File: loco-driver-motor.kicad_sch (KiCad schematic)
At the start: 20 parts, among them U901 BDR6133

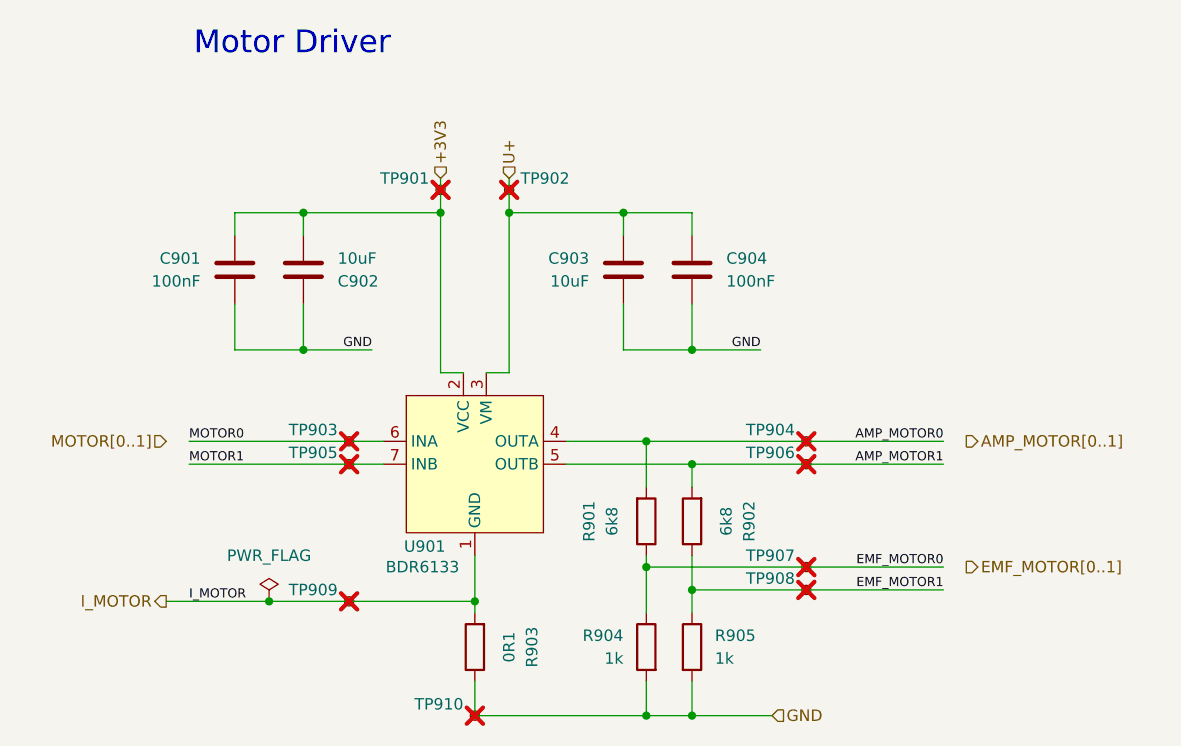
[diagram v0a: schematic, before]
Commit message: Fix - revert to working model
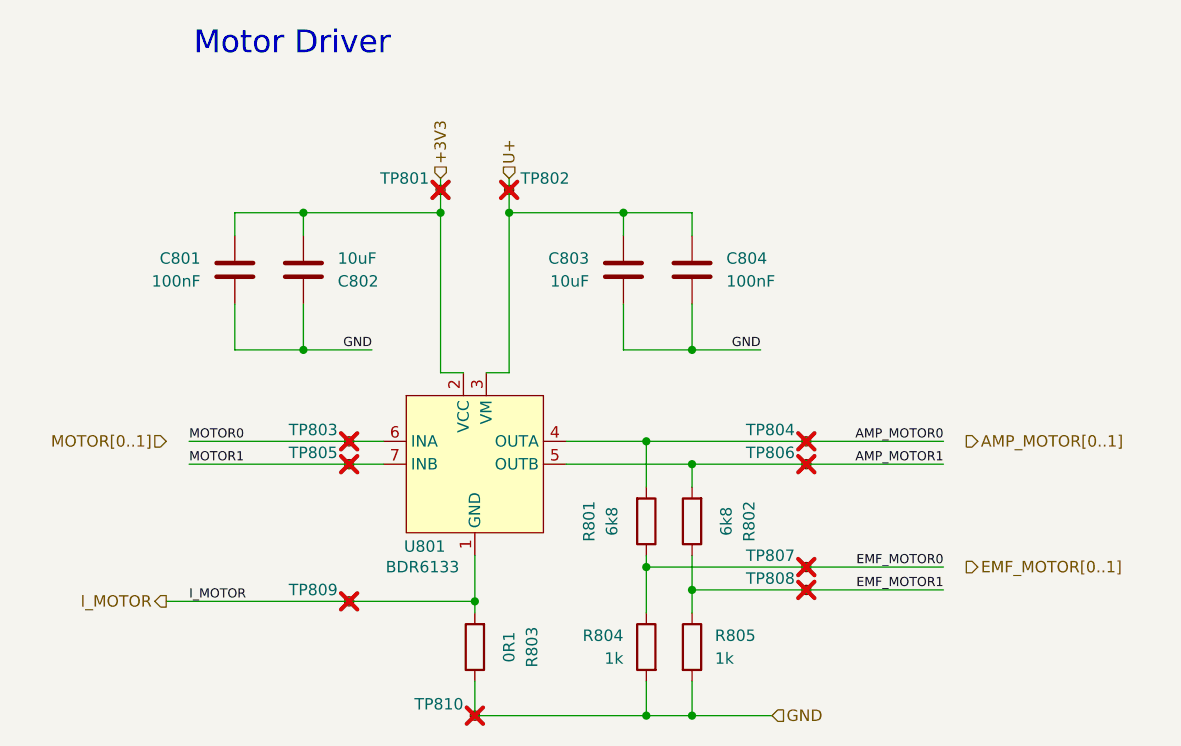
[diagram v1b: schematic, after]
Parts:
- renumbered C901 to C801, C902 to C802, C903 to C803, C904 to C804, R901 to R801, R902 to R802, R903 to R803, R904 to R804, R905 to R805, TP901 to TP801, TP902 to TP802, TP903 to TP803, TP904 to TP804, TP905 to TP805, TP906 to TP806, TP907 to TP807, TP908 to TP808, TP909 to TP809, TP910 to TP810, U901 to U801
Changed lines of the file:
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@@
-	)
-	(junction
-		(at 43.18 91.44)
-		(diameter 0)
-		(color 0 0 0 0)
 	)
 	(junction
@@
 	(wire
 		(pts
-			(xy 43.18 91.44) (xy 52.07 91.44)
-		)
-		(stroke
-			(width 0)
-			(type default)
-		)
-	)
-	(wire
-		(pts
 			(xy 66.04 100.33) (xy 66.04 104.14)
 		)
@@
 	(wire
 		(pts
-			(xy 31.75 91.44) (xy 43.18 91.44)
+			(xy 31.75 91.44) (xy 52.07 91.44)
 		)
 		(stroke
@@
 		(on_board no)
 		(dnp yes)
-		(property "Reference" "TP906"
+		(property "Reference" "TP806"
 			(at 101.6 74.9299 0)
 			(effects
@@
 			(project "xDuinoRails-Thor-M"
 				(path "/fb33ec4e-6596-45d2-a121-8d3475acd69a/28e0fa6a-354f-41d6-8b58-d1dd784eb1fe"
-					(reference "TP906")
+					(reference "TP806")
 					(unit 1)
 				)
@@
 		(on_board yes)
 		(dnp no)
-		(property "Reference" "U901"
+		(property "Reference" "U801"
 			(at 58.166 85.344 0)
 			(effects
@@
 			(project "xDuinoRails-Thor-M"
 				(path "/fb33ec4e-6596-45d2-a121-8d3475acd69a/28e0fa6a-354f-41d6-8b58-d1dd784eb1fe"
-					(reference "U901")
+					(reference "U801")
 					(unit 1)
 				)
@@
 		(on_board yes)
 		(dnp no)
-		(property "Reference" "R903"
+		(property "Reference" "R803"
 			(at 72.39 96.52 90)
 			(effects
@@
 			(project "xDuinoRails-Thor-M"
 				(path "/fb33ec4e-6596-45d2-a121-8d3475acd69a/28e0fa6a-354f-41d6-8b58-d1dd784eb1fe"
-					(reference "R903")
+					(reference "R803")
 					(unit 1)
 				)
@@
 		(on_board yes)
 		(dnp no)
-		(property "Reference" "R902"
+		(property "Reference" "R802"
 			(at 96.52 82.55 90)
 			(effects
@@
 			(project "xDuinoRails-Thor-M"
 				(path "/fb33ec4e-6596-45d2-a121-8d3475acd69a/28e0fa6a-354f-41d6-8b58-d1dd784eb1fe"
-					(reference "R902")
-					(unit 1)
-				)
-			)
-		)
-	)
-	(symbol
-		(lib_id "power:PWR_FLAG")
-		(at 43.18 91.44 0)
-		(unit 1)
-		(exclude_from_sim no)
-		(in_bom yes)
-		(on_board yes)
-		(dnp no)
-		(fields_autoplaced yes)
-		(property "Reference" "#FLG901"
-			(at 43.18 89.535 0)
-			(effects
-				(font
-					(size 1.27 1.27)
-				)
-				(hide yes)
-			)
-		)
-		(property "Value" "PWR_FLAG"
-			(at 43.18 86.36 0)
-			(effects
-				(font
-					(size 1.27 1.27)
-				)
-			)
-		)
-		(property "Footprint" ""
-			(at 43.18 91.44 0)
-			(effects
-				(font
-					(size 1.27 1.27)
-				)
-				(hide yes)
-			)
-		)
-		(property "Datasheet" "~"
-			(at 43.18 91.44 0)
-			(effects
-				(font
-					(size 1.27 1.27)
-				)
-				(hide yes)
-			)
-		)
-		(property "Description" "Special symbol for telling ERC where power comes from"
-			(at 43.18 91.44 0)
-			(effects
-				(font
-					(size 1.27 1.27)
-				)
-				(hide yes)
-			)
-		)
-		(pin "1"
-		)
-		(instances
-			(project ""
-				(path "/fb33ec4e-6596-45d2-a121-8d3475acd69a/28e0fa6a-354f-41d6-8b58-d1dd784eb1fe"
-					(reference "#FLG901")
+					(reference "R802")
 					(unit 1)
 				)
@@
 		(on_board no)
 		(dnp yes)
-		(property "Reference" "TP909"
+		(property "Reference" "TP809"
 			(at 50.8 90.1699 0)
 			(effects
@@
 			(project "xDuinoRails-Thor-M"
 				(path "/fb33ec4e-6596-45d2-a121-8d3475acd69a/28e0fa6a-354f-41d6-8b58-d1dd784eb1fe"
-					(reference "TP909")
+					(reference "TP809")
 					(unit 1)
 				)
@@
 		(dnp no)
 		(fields_autoplaced yes)
-		(property "Reference" "R901"
+		(property "Reference" "R801"
 			(at 78.74 82.55 90)
 			(effects
@@
 			(project "xDuinoRails-Thor-M"
 				(path "/fb33ec4e-6596-45d2-a121-8d3475acd69a/28e0fa6a-354f-41d6-8b58-d1dd784eb1fe"
-					(reference "R901")
+					(reference "R801")
 					(unit 1)
 				)
@@
 		(on_board no)
 		(dnp yes)
-		(property "Reference" "TP904"
+		(property "Reference" "TP804"
 			(at 101.6 72.3899 0)
 			(effects
@@
 			(project "xDuinoRails-Thor-M"
 				(path "/fb33ec4e-6596-45d2-a121-8d3475acd69a/28e0fa6a-354f-41d6-8b58-d1dd784eb1fe"
-					(reference "TP904")
+					(reference "TP804")
 					(unit 1)
 				)
@@
 		(on_board no)
 		(dnp yes)
-		(property "Reference" "TP908"
+		(property "Reference" "TP808"
 			(at 101.6 88.8999 0)
 			(effects
@@
 			(project "xDuinoRails-Thor-M"
 				(path "/fb33ec4e-6596-45d2-a121-8d3475acd69a/28e0fa6a-354f-41d6-8b58-d1dd784eb1fe"
-					(reference "TP908")
+					(reference "TP808")
 					(unit 1)
 				)
@@
 		(on_board no)
 		(dnp yes)
-		(property "Reference" "TP902"
+		(property "Reference" "TP802"
 			(at 71.12 44.4499 0)
 			(effects
@@
 			(project "xDuinoRails-Thor-M"
 				(path "/fb33ec4e-6596-45d2-a121-8d3475acd69a/28e0fa6a-354f-41d6-8b58-d1dd784eb1fe"
-					(reference "TP902")
+					(reference "TP802")
 					(unit 1)
 				)
@@
 		(dnp no)
 		(fields_autoplaced yes)
-		(property "Reference" "C904"
+		(property "Reference" "C804"
 			(at 93.98 53.3399 0)
 			(effects
@@
 			(project "xDuinoRails-Thor-M"
 				(path "/fb33ec4e-6596-45d2-a121-8d3475acd69a/28e0fa6a-354f-41d6-8b58-d1dd784eb1fe"
-					(reference "C904")
+					(reference "C804")
 					(unit 1)
 				)
@@
 		(on_board no)
 		(dnp yes)
-		(property "Reference" "TP901"
+		(property "Reference" "TP801"
 			(at 60.96 44.4499 0)
 			(effects
@@
 			(project "xDuinoRails-Thor-M"
 				(path "/fb33ec4e-6596-45d2-a121-8d3475acd69a/28e0fa6a-354f-41d6-8b58-d1dd784eb1fe"
-					(reference "TP901")
+					(reference "TP801")
 					(unit 1)
 				)
@@
 		(dnp no)
 		(fields_autoplaced yes)
-		(property "Reference" "R904"
+		(property "Reference" "R804"
 			(at 82.55 95.2499 0)
 			(effects
@@
 			(project "xDuinoRails-Thor-M"
 				(path "/fb33ec4e-6596-45d2-a121-8d3475acd69a/28e0fa6a-354f-41d6-8b58-d1dd784eb1fe"
-					(reference "R904")
+					(reference "R804")
 					(unit 1)
 				)
@@
 		(on_board no)
 		(dnp yes)
-		(property "Reference" "TP903"
+		(property "Reference" "TP803"
 			(at 50.8 72.3899 0)
 			(effects
@@
 			(project "xDuinoRails-Thor-M"
 				(path "/fb33ec4e-6596-45d2-a121-8d3475acd69a/28e0fa6a-354f-41d6-8b58-d1dd784eb1fe"
-					(reference "TP903")
+					(reference "TP803")
 					(unit 1)
 				)
@@
 		(on_board yes)
 		(dnp no)
-		(property "Reference" "C903"
+		(property "Reference" "C803"
 			(at 78.74 53.3399 0)
 			(effects
@@
 			(project "xDuinoRails-Thor-M"
 				(path "/fb33ec4e-6596-45d2-a121-8d3475acd69a/28e0fa6a-354f-41d6-8b58-d1dd784eb1fe"
-					(reference "C903")
+					(reference "C803")
 					(unit 1)
 				)
@@
 		(on_board no)
 		(dnp yes)
-		(property "Reference" "TP907"
+		(property "Reference" "TP807"
 			(at 101.6 86.3599 0)
 			(effects
@@
 			(project "xDuinoRails-Thor-M"
 				(path "/fb33ec4e-6596-45d2-a121-8d3475acd69a/28e0fa6a-354f-41d6-8b58-d1dd784eb1fe"
-					(reference "TP907")
+					(reference "TP807")
 					(unit 1)
 				)
@@
 		(on_board no)
 		(dnp yes)
-		(property "Reference" "TP910"
+		(property "Reference" "TP810"
 			(at 64.77 102.8699 0)
 			(effects
@@
 			(project "xDuinoRails-Thor-M"
 				(path "/fb33ec4e-6596-45d2-a121-8d3475acd69a/28e0fa6a-354f-41d6-8b58-d1dd784eb1fe"
-					(reference "TP910")
+					(reference "TP810")
 					(unit 1)
 				)
@@
 		(dnp no)
 		(fields_autoplaced yes)
-		(property "Reference" "C901"
+		(property "Reference" "C801"
 			(at 35.56 53.3399 0)
 			(effects
@@
 			(project "xDuinoRails-Thor-M"
 				(path "/fb33ec4e-6596-45d2-a121-8d3475acd69a/28e0fa6a-354f-41d6-8b58-d1dd784eb1fe"
-					(reference "C901")
+					(reference "C801")
 					(unit 1)
 				)
@@
 		(on_board yes)
 		(dnp no)
-		(property "Reference" "C902"
+		(property "Reference" "C802"
 			(at 50.8 55.8801 0)
 			(effects
@@
 			(project "xDuinoRails-Thor-M"
 				(path "/fb33ec4e-6596-45d2-a121-8d3475acd69a/28e0fa6a-354f-41d6-8b58-d1dd784eb1fe"
-					(reference "C902")
+					(reference "C802")
 					(unit 1)
 				)
@@
 		(on_board no)
 		(dnp yes)
-		(property "Reference" "TP905"
+		(property "Reference" "TP805"
 			(at 50.8 74.9299 0)
 			(effects
@@
 			(project "xDuinoRails-Thor-M"
 				(path "/fb33ec4e-6596-45d2-a121-8d3475acd69a/28e0fa6a-354f-41d6-8b58-d1dd784eb1fe"
-					(reference "TP905")
+					(reference "TP805")
 					(unit 1)
 				)
@@
 		(on_board yes)
 		(dnp no)
-		(property "Reference" "R905"
+		(property "Reference" "R805"
 			(at 92.71 95.2499 0)
 			(effects
@@
 			(project "xDuinoRails-Thor-M"
 				(path "/fb33ec4e-6596-45d2-a121-8d3475acd69a/28e0fa6a-354f-41d6-8b58-d1dd784eb1fe"
-					(reference "R905")
+					(reference "R805")
 					(unit 1)
 				)

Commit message: Add - Fix ERC errors
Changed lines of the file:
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@@
+	)
+	(junction
+		(at 54.61 91.44)
+		(diameter 0)
+		(color 0 0 0 0)
 	)
 	(junction
@@
 	(wire
 		(pts
-			(xy 52.07 91.44) (xy 66.04 91.44)
-		)
-		(stroke
-			(width 0)
-			(type default)
-		)
-	)
-	(wire
-		(pts
 			(xy 90.17 86.36) (xy 90.17 90.17)
 		)
@@
 	(wire
 		(pts
+			(xy 54.61 91.44) (xy 52.07 91.44)
+		)
+		(stroke
+			(width 0)
+			(type default)
+		)
+	)
+	(wire
+		(pts
 			(xy 66.04 86.36) (xy 66.04 91.44)
 		)
@@
 		(pts
 			(xy 39.37 50.8) (xy 39.37 48.26)
+		)
+		(stroke
+			(width 0)
+			(type default)
+		)
+	)
+	(wire
+		(pts
+			(xy 54.61 91.44) (xy 66.04 91.44)
 		)
 		(stroke
@@
 					(unit 1)
 				)
+			)
+		)
+	)
+	(symbol
+		(lib_id "power:PWR_FLAG")
+		(at 54.61 91.44 180)
+		(unit 1)
+		(exclude_from_sim no)
+		(in_bom yes)
+		(on_board yes)
+		(dnp no)
+		(property "Reference" "#FLG801"
+			(at 54.61 93.345 0)
+			(effects
+				(font
+					(size 1.27 1.27)
+				)
+				(hide yes)
+			)
+		)
+		(property "Value" "PWR_FLAG"
+			(at 54.61 96.52 0)
+			(effects
+				(font
+					(size 1.27 1.27)
+				)
+			)
+		)
+		(property "Footprint" ""
+			(at 54.61 91.44 0)
+			(effects
+				(font
+					(size 1.27 1.27)
+				)
+				(hide yes)
+			)
+		)
+		(property "Datasheet" "~"
+			(at 54.61 91.44 0)
+			(effects
+				(font
+					(size 1.27 1.27)
+				)
+				(hide yes)
+			)
+		)
+		(property "Description" "Special symbol for telling ERC where power comes from"
+			(at 54.61 91.44 0)
+			(effects
+				(font
+					(size 1.27 1.27)
+				)
+				(hide yes)
+			)
+		)
+		(pin "1"
+		)
+		(instances
+			(project ""
+				(path "/fb33ec4e-6596-45d2-a121-8d3475acd69a/28e0fa6a-354f-41d6-8b58-d1dd784eb1fe"
+					(reference "#FLG801")
+					(unit 1)
+				)
